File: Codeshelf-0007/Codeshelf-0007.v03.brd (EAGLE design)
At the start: 140.1 x 99 mm, 53 parts, among them J1 M05X2PTH, J2 RJ45-8PTH, J3-WAKE M02PTH, J4 RJ45-8PTH, J5 HEADER-2X-2.54MM, U1 ZSFM201-1A, U2 MAX232SOIC16, U3 RS485SOIC, U4 ULN2003AD, U5 MIC94061C6, U6 MIC94061C6

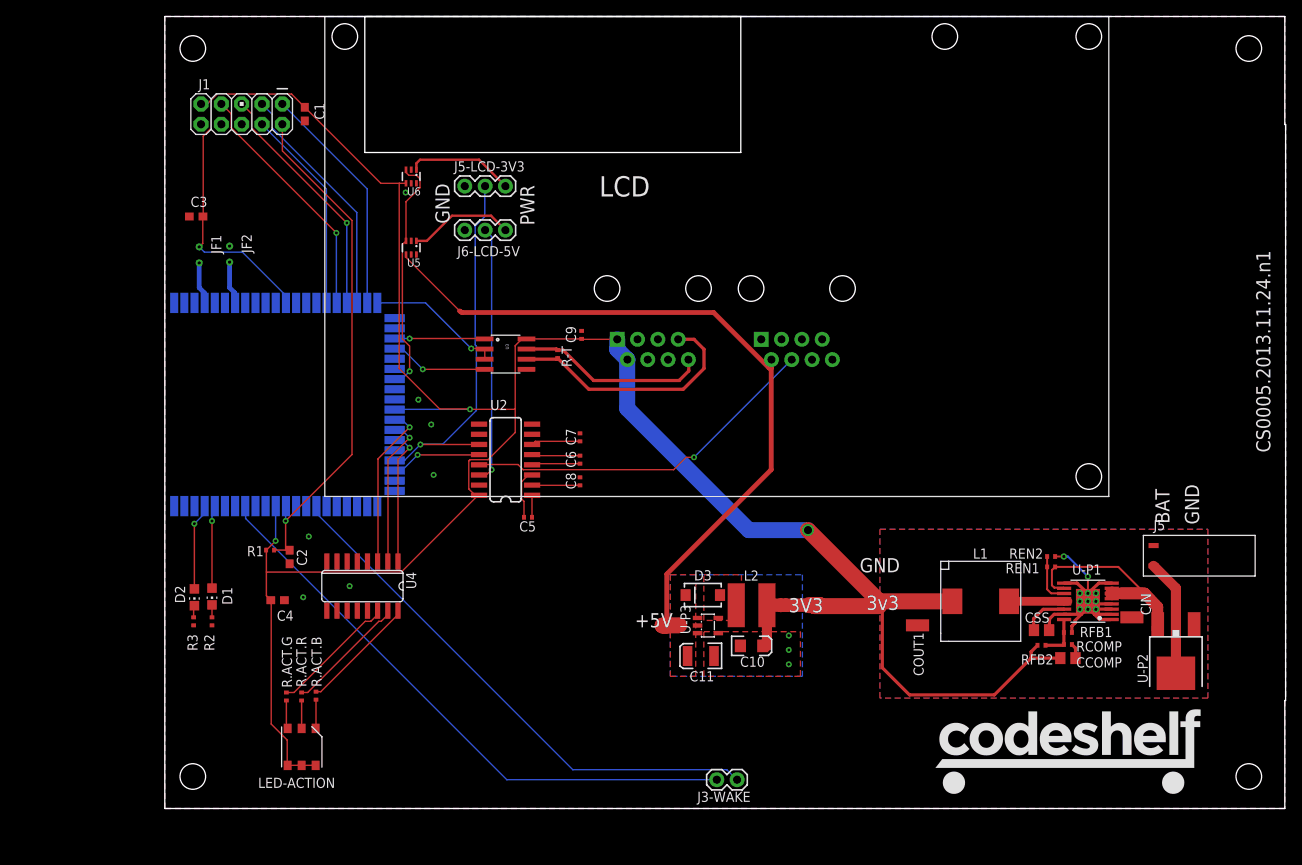
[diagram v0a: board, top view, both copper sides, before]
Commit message: New position controller design
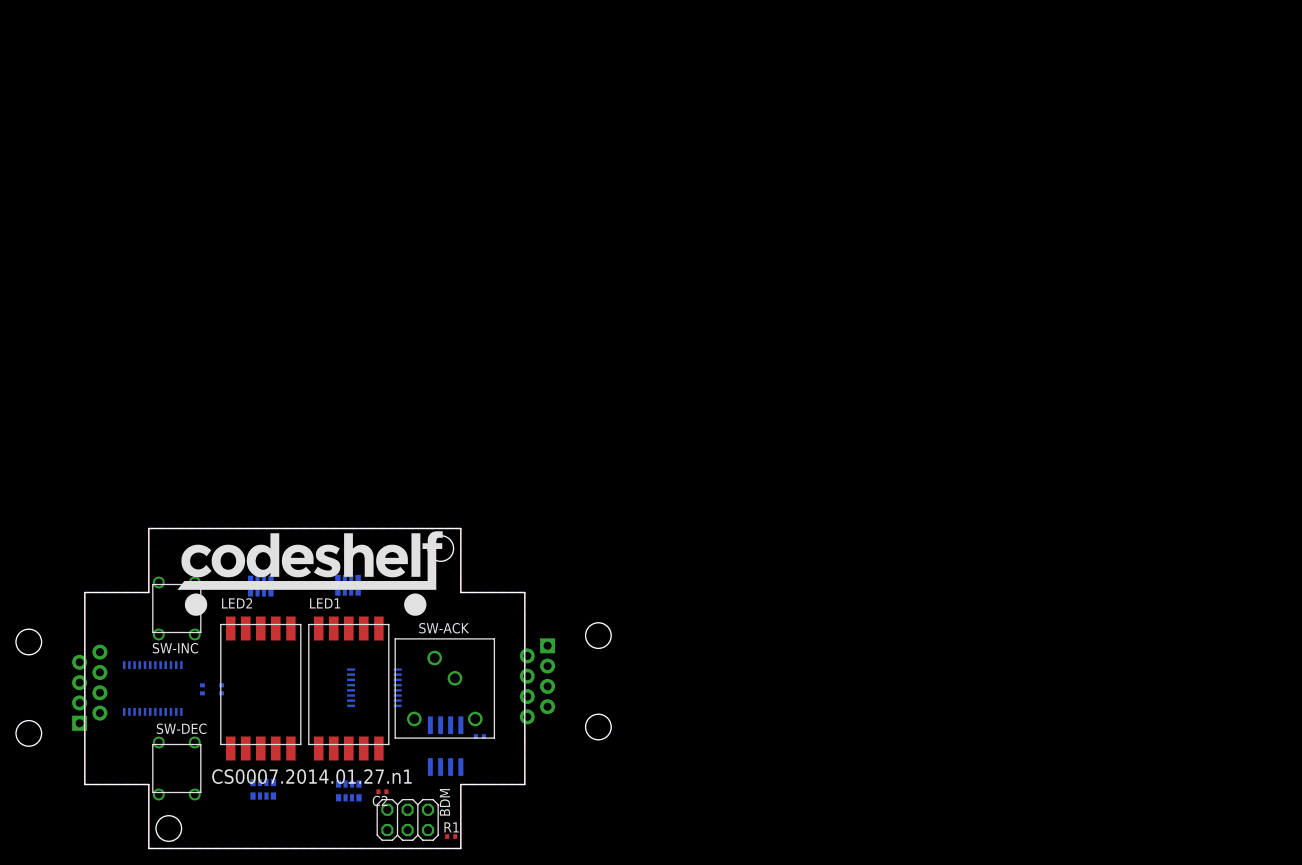
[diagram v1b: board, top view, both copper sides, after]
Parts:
- removed C10: 10uF, SparkFun:EIA3216
- removed C11: 68uF, SparkFun:EIA3528
- removed C3, C4: 100pF, GW-devices:C0603
- removed C5, C6, C7, C8, C9: .1uF, GW-devices:C0402
- removed CCOMP: 68pF, GW-devices:C0805
- removed CIN: 47uF, GW-devices:C1210K
- removed COUT1: 100uF, GW-devices:C1210K
- removed CSS: 2.7nF, GW-devices:C0805
- removed D1: RED, led:CHIP-LED0805
- removed D2: GREEN, led:CHIP-LED0805
- removed D3: MBRA140, SparkFun:SMA-DIODE
- removed J3-WAKE: M02PTH, SparkFun-Connectors:1X02
- removed J4: RJ45-8PTH, SparkFun:RJ45-8
- removed J5: HEADER-2X-2.54MM, GW-devices:HEADER-2X-RA-2.54MM
- removed J5-LCD-3V3, J6-LCD-5V: (no value), SparkFun-Connectors:1X03
- removed JF1, JF2: JUMPER-2X-SMT-VIA, GW-devices:JUMPER-VIA-2X
- removed L1: 150uH, GW-devices:SLF10165
- removed L2: 47uH, SparkFun:CR54
- removed LCD: LCD-SPARKFUN, GW-devices:LCD-20X4-SPARKFUN
- removed LED-ACTION: LED5060A, GW-devices:PLCC-6
- removed R-T: 120, GW-devices:RF-R0402
- removed R.ACT.B, R.ACT.G: 10, GW-devices:RF-R0402
- removed R.ACT.R: 68, GW-devices:RF-R0402
- removed RCOMP: 4.64K, GW-devices:RF-R0402
- removed REN1: 22K, GW-devices:RF-R0402
- removed REN2: 10K, GW-devices:RF-R0402
- removed RFB1: 45.3K, GW-devices:RF-R0402
- removed RFB2: 143K, GW-devices:RF-R0402
- removed U-P1: LM2854MH, GW-devices:HTSSOP16PWP
- removed U-P2: PCHANNEL-MOSFET-DPAK, GW-devices:DPAK
- removed U-P3: NCP1402, SparkFun:SOT23-5
- removed U1: ZSFM201-1A, GW-devices:ZSFM201-1
- removed U5, U6: MIC94061C6, GW-devices:SC70-6L
- added ACK.BUTTON.KEYCAP, CASE, STANDOFF1, STANDOFF2, STANDOFF3, STANDOFF4: EXTERNAL-COMPONENT, GW-devices:EXTERNAL-COMPONENT
- added BDM: HEADER-3X2, GW-devices:HEADER-3X2
- added LED1, LED2: 7SEGMENT-1DIGITSMD, GW-devices:7SEGMENT-1DIG-.40-SMD
- added R.D2A, R.D2B, R.D2C, R.D2D: RESISTOR-ARRAY-4X-3216, GW-devices:3216-4X
- added SW-ACK: SWITCH-TACTILE-320.03E11, GW-devices:SWITCH-TACTILE-320.03E11
- added SW-DEC, SW-INC: SWITCH-TACTILE-FSM, GW-devices:SWITCH-TACTILE-FSM
- C1: value 100pF -> .1uF; device GW-devices:C0603 -> GW-devices:C0402
- C2: value 1nF -> .1uF; device GW-devices:C0603 -> GW-devices:C0402
- J1: value M05X2PTH -> RJ45-8PTH; device SparkFun:AVR_ICSP -> GW-devices:RJ45-8
- J2: device SparkFun:RJ45-8 -> GW-devices:RJ45-8
- R1: value 100K -> 3.3K
- R2: value 220 -> 10K
- R3: value 390 -> 10K
- U2: value MAX232SOIC16 -> MC9S08QG-DT; device SparkFun:SO016 -> GW-devices:TSSOP16
- U3: value RS485SOIC -> CAT9552; device SparkFun:SO08 -> GW-devices:TSSOP24
- U4: value ULN2003AD -> RS485SOIC; device uln-udn:SO16 -> SparkFun:SO08
- moved J2 108.2 mm to (-7.00, 20.1), turned to 90 degrees
- moved LOGO 97.3 mm to (11.6, 29.1)
- moved J1 83.8 mm to (64.2, 20.9), flipped to the bottom
- moved C1 80.8 mm to (49.4, 14.0), flipped to the bottom, turned to 0 degrees
- moved U3 60.8 mm to (8.50, 20.0), flipped to the bottom, turned to 180 degrees
- moved R1 42.4 mm to (45.8, 1.50), turned to 0 degrees
- moved U2 32.9 mm to (36.2, 20.1), flipped to the bottom
- moved C2 31.5 mm to (37.2, 7.10), turned to 0 degrees
- moved U4 22.5 mm to (45.1, 12.8), flipped to the bottom
- moved R2 8.58 mm to (17.1, 19.9), flipped to the bottom
- moved R3 8.57 mm to (14.7, 19.9), flipped to the bottom
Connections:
- removed net +5V: C11.A, D3.C, J2.2, U-P3.1, U-P3.2, U5.4
- removed net C1: C5.1, U2.1
- removed net C2: C6.1, U2.4
- removed net N$39: U1.32, U4.3
- removed net R1IN: J2.4, U2.13
- removed net R1OUT: U1.37, U2.12
- removed net RTCK: J1.4, U1.16
- removed net T1IN: J5-LCD-3V3.2, U1.36, U2.11
- removed net T1OUT: J6-LCD-5V.2, U2.14
- removed net TCK: J1.3, U1.19
- removed net TDI: J1.5, U1.18
- removed net TDO: J1.7, U1.17
- removed net TMS: J1.1, U1.20
- removed net V-PROT: CIN.1, REN1.2, U-P1.10, U-P1.5, U-P1.6, U-P1.7, U-P2.3
- removed net VBATT: J5.2, U-P2.4
- new net N$27: LED1.5, R.D2C.8
- new net N$29: LED1.2, R.D2C.6
- new net N$31: R.D2D.4, U3.13
- new net N$32: R.D2D.3, U3.14
- new net RS485_N: J1.8, J2.8, U4.7
- new net RS485_P: J1.7, J2.7, U4.6
- new net RX: U2.12, U4.1
- new net SLA: R2.1, U2.14, U3.23
- new net SLC: R3.1, U2.13, U3.22
- new net TX: U2.11, U4.4
- net +3V3: now also BDM.6, J1.1, J1.2, J2.1, J2.2, LED1.3, LED1.8, LED2.3, LED2.8, R2.2, R3.2, U2.3, U3.24, U4.8; no longer C10.A, C3.2, C4.2, C9.1, CCOMP.2, COUT1.1, J1.9, J4.1, J4.2, JF1.1, L1.2, L2.P$1, LED-ACTION.4, LED-ACTION.5, LED-ACTION.6, RFB2.2, U1.12, U1.31, U1.50, U2.16, U3.8, U6.4
- net GND: now also BDM.2, C2.1, J1.3, J1.6, J2.6, SW-ACK.P$3, SW-ACK.P$4, SW-DEC.P$3, SW-DEC.P$4, SW-INC.P$3, SW-INC.P$4, U2.4, U3.1, U3.12, U3.2, U3.3, U4.5; no longer C10.C, C11.C, C2.2, C3.1, C4.1, C7.2, C8.2, C9.2, CIN.2, COUT1.2, CSS.2, J1.10, J4.3, J4.6, J5-LCD-3V3.1, J5.1, J6-LCD-5V.1, JF2.1, R2.1, R3.1, REN2.1, RFB1.1, U-P1.1, U-P1.15, U-P1.2, U-P1.3, U-P1.4, U-P1.8, U-P1.9, U-P1.EXP, U-P2.1, U-P3.4, U1.1, U1.2, U1.22, U1.3, U1.38, U1.51, U1.58, U1.59, U1.60, U2.15, U3.5, U4.8, U5.2, U5.5, U6.2, U6.5
- net N$1: now also R.D2A.5, U3.11; no longer D2.A, U1.57
- net N$10: now also R.D2B.6, U3.6; no longer J5-LCD-3V3.3, U6.1
- net N$11: now also R.D2B.7, U3.5; no longer C6.2, U2.5
- net N$12: now also R.D2B.8, U3.4; no longer C7.1, U2.6
- net N$13: now also LED2.6, R.D2A.1; no longer J6-LCD-5V.3, U5.1
- net N$14: now also LED2.7, R.D2A.2; no longer J3-WAKE.2, U1.46
- net N$15: now also LED2.9, R.D2A.3; no longer C8.1, U2.2
- net N$16: now also LED2.10, R.D2A.4; no longer J3-WAKE.1, U1.53
- net N$17: now also LED2.5, R.D2D.8; no longer U1.25, U3.4
- net N$18: now also LED2.4, R.D2D.7; no longer U1.24, U3.1
- net N$19: now also U2.9, U4.2, U4.3; no longer U1.21, U3.2, U3.3
- net N$2: now also R.D2A.6, U3.10; no longer D1.A, U1.56
- net N$20: now also LED2.2, R.D2D.6; no longer J4.8, R-T.1, U3.7
- net N$21: now also LED2.1, R.D2D.5; no longer J4.7, R-T.2, U3.6
- net N$22: now also LED1.6, R.D2B.1; no longer CSS.1, U-P1.14
- net N$23: now also BDM.4, C2.2, U2.1; no longer L1.1, U-P1.12, U-P1.13
- net N$24: now also LED1.7, R.D2B.2; no longer RCOMP.2, RFB1.2, RFB2.1, U-P1.16
- net N$25: now also LED1.9, R.D2B.3; no longer CCOMP.1, RCOMP.1
- net N$26: now also LED1.10, R.D2B.4; no longer REN1.1, REN2.2, U-P1.11
- net N$28: now also LED1.4, R.D2C.7; no longer R.ACT.R.2, U4.15
- net N$3: now also R.D2A.7, U3.9; no longer D2.C, R3.2
- net N$30: now also LED1.1, R.D2C.5; no longer R.ACT.G.2, U4.14
- net N$33: now also R.D2D.2, U3.15; no longer LED-ACTION.1, R.ACT.B.1
- net N$34: now also R.D2D.1, U3.16; no longer LED-ACTION.2, R.ACT.R.1
- net N$35: now also R.D2C.4, U3.17; no longer LED-ACTION.3, R.ACT.G.1
- net N$36: now also R.D2C.3, U3.18; no longer U1.34, U4.1
- net N$37: now also R.D2C.2, U3.19; no longer U1.33, U4.2
- net N$38: now also R.D2C.1, U3.20; no longer R.ACT.B.2, U4.16
- net N$4: now also R.D2A.8, U3.8; no longer D1.C, R2.2
- net N$5: now also R.D2B.5, U3.7; no longer D3.A, L2.P$2, U-P3.5
- net N$6: now also SW-ACK.P$1, SW-ACK.P$2, U2.16; no longer JF2.2, U1.7
- net N$7: now also SW-DEC.P$1, SW-DEC.P$2, U2.15; no longer JF1.2, U1.4
- net N$8: now also SW-INC.P$1, SW-INC.P$2, U2.10; no longer C5.2, U2.3
- net N$9: now also BDM.1, R1.1, U2.2; no longer U1.28, U5.3, U6.3
- net RESET: now also U2.7, U3.21; no longer C2.1, J1.2, R1.1, U1.49
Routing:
- net +3V3: track 349.7 -> 0.00 mm, vias 3 -> 0
- net GND: track 45.5 -> 190.0 mm, vias 21 -> 0
- net +5V: track 93.0 -> 0.00 mm
- net N$16: track 74.0 -> 0.00 mm
- net N$14: track 67.3 -> 0.00 mm
- net RESET: track 64.1 -> 0.00 mm, vias 1 -> 0
- net T1IN: track 48.8 -> 0.00 mm, vias 1 -> 0
- net R1IN: track 45.1 -> 0.00 mm, vias 1 -> 0
- net T1OUT: track 32.1 -> 0.00 mm, vias 1 -> 0
- net N$21: track 31.1 -> 0.00 mm
- net TDO: track 30.9 -> 0.00 mm, vias 1 -> 0
- net TDI: track 30.3 -> 0.00 mm, vias 1 -> 0
- net N$9: track 30.0 -> 0.00 mm, vias 1 -> 0
- net TCK: track 29.8 -> 0.00 mm
- net TMS: track 29.3 -> 0.00 mm
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- removed copper zone on layer 1, net +5V
- removed copper zone on layer 16, net GND
- removed copper zone on layer 1, net N$5
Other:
- board size 140.1 x 99 mm -> 55 x 40 mm
- board text added: "CS0007.2014.01.27.n1"
- board text removed: "+5V"
- board text removed: "3V3"
- board text removed: "3v3"
- board text removed: "BAT"
- board text removed: "CS0005.2013.11.24.n1"
- board text removed: "GND"
- board text removed: "PWR"
